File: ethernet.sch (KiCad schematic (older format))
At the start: 23 parts, among them U4 LAN8710A-EZC, U5 ARJM11C7-114-BA

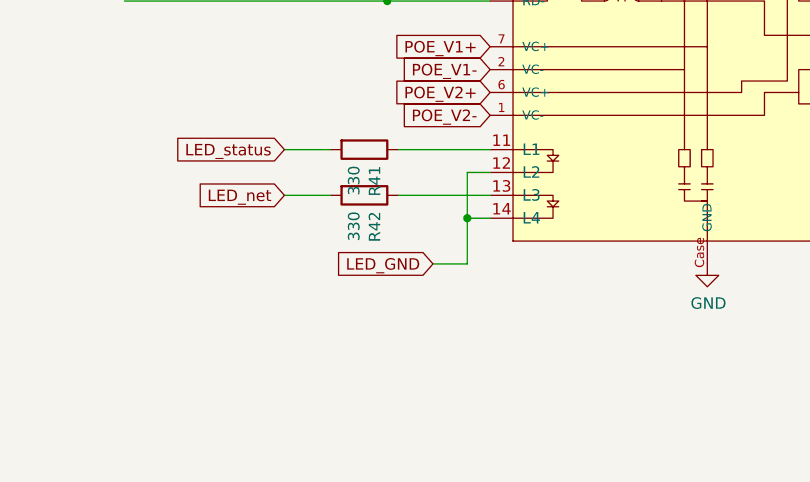
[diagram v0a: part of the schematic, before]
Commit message: Adjust front IO to work with a flush panel
also removed the LED enable transistor
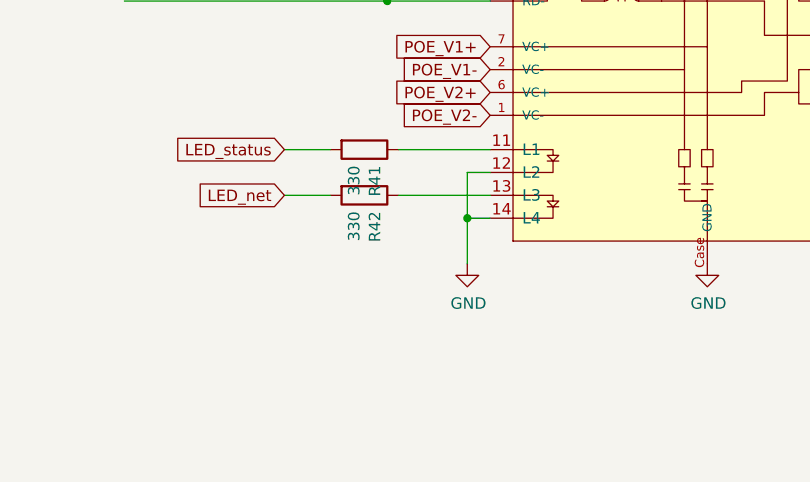
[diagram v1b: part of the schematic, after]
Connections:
- net LED_GND is gone; now on net GND: U5.12 (L2), U5.14 (L4)
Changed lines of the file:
@@
 Wire Wire Line
 	8800 5300 8800 5500
-Text GLabel 8650 5500 0    50   Input ~ 0
-LED_GND
-Wire Wire Line
-	8650 5500 8800 5500
 Wire Wire Line
 	8000 5000 8200 5000
@@
 Text GLabel 5550 3000 0    50   Input ~ 0
 LED_status
+$Comp
+L power:GND #PWR?
+U 1 1 612DAEC9
+P 8800 5500
+F 0 "#PWR?" H 8800 5250 50  0001 C CNN
+F 1 "GND" H 8805 5327 50  0000 C CNN
+F 2 "" H 8800 5500 50  0001 C CNN
+F 3 "" H 8800 5500 50  0001 C CNN
+	1    8800 5500
+	1    0    0    -1
+$EndComp
 $EndSCHEMATC
